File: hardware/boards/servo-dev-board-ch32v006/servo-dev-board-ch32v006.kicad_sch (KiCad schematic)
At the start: 87 parts, among them J1 BATT JST-PH, J2 BUS JST-ZH, J3 BUS JST-ZH, J4 SERVO JST-ZH, J5 ENC JST-ZH, J6 DBG JST-ZH, Q1 AO3401A, Q2 AO3401A, Q3 AO3401A, SW1 SW_Push, U1 TPAP2210K-3.3TRG1, U2 74LVC2G125RA3-7, U3 DRV8837DSGR-JSM, U4 CH32V006F8U6

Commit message: wip
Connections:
- net DATA: now also TP17.1; no longer TP4.1
- net DBG: now also TP16.1; no longer TP2.1
- net EN: now also TP14.1; no longer TP7.1
- net ENCA: now also TP8.1; no longer TP18.1
- net ENCB: now also TP9.1; no longer TP19.1
- net IN1: now also TP2.1; no longer TP5.1
- net IN2: now also TP3.1; no longer TP6.1
- net RX: now also TP18.1; no longer TP9.1
- net TX: now also TP19.1; no longer TP8.1
- net VNTC: now also TP7.1; no longer TP15.1
- net VPOS: now also TP6.1; no longer TP14.1
- net VSNA: now also TP4.1; no longer TP16.1
- net VSNB: now also TP5.1; no longer TP17.1
- net LED renamed STAT
- net STAT: now also TP15.1; no longer TP3.1
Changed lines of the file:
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@@
 	(wire
 		(pts
-			(xy 147.32 142.24) (xy 147.32 138.43)
+			(xy 147.32 142.24) (xy 147.32 135.89)
 		)
 		(stroke
@@
 		)
 	)
-	(label "LED"
-		(at 147.32 138.43 0)
-		(effects
-			(font
-				(size 1.27 1.27)
-			)
-			(justify left bottom)
+	(label "STAT"
+		(at 147.32 135.89 270)
+		(effects
+			(font
+				(size 1.27 1.27)
+			)
+			(justify right bottom)
 		)
 	)
@@
 		)
 	)
+	(label "RX"
+		(at 229.87 40.64 0)
+		(effects
+			(font
+				(size 1.27 1.27)
+			)
+			(justify left bottom)
+		)
+	)
+	(label "ENCB"
+		(at 226.06 43.18 180)
+		(effects
+			(font
+				(size 1.27 1.27)
+			)
+			(justify right bottom)
+		)
+	)
 	(label "ENCA"
 		(at 256.54 91.44 180)
@@
 		)
 	)
+	(label "VSNA"
+		(at 226.06 30.48 180)
+		(effects
+			(font
+				(size 1.27 1.27)
+			)
+			(justify right bottom)
+		)
+	)
 	(label "ISNS+"
 		(at 257.81 140.97 180)
@@
 	)
 	(label "ENCA"
-		(at 229.87 40.64 0)
-		(effects
-			(font
-				(size 1.27 1.27)
-			)
-			(justify left bottom)
+		(at 226.06 40.64 180)
+		(effects
+			(font
+				(size 1.27 1.27)
+			)
+			(justify right bottom)
 		)
 	)
@@
 		)
 	)
-	(label "ENCB"
-		(at 229.87 43.18 0)
-		(effects
-			(font
-				(size 1.27 1.27)
-			)
-			(justify left bottom)
-		)
-	)
-	(label "VPOS"
-		(at 229.87 30.48 0)
-		(effects
-			(font
-				(size 1.27 1.27)
-			)
-			(justify left bottom)
-		)
-	)
 	(label "VNTC"
 		(at 256.54 93.98 180)
@@
 		)
 	)
-	(label "DBG"
-		(at 226.06 25.4 180)
-		(effects
-			(font
-				(size 1.27 1.27)
-			)
-			(justify right bottom)
-		)
-	)
-	(label "DATA"
-		(at 226.06 30.48 180)
-		(effects
-			(font
-				(size 1.27 1.27)
-			)
-			(justify right bottom)
-		)
-	)
-	(label "LED"
+	(label "STAT"
 		(at 187.96 106.68 0)
 		(effects
@@
 		)
 	)
-	(label "LED"
-		(at 226.06 27.94 180)
+	(label "VPOS"
+		(at 226.06 35.56 180)
 		(effects
 			(font
@@
 		)
 	)
-	(label "IN1"
-		(at 226.06 33.02 180)
-		(effects
-			(font
-				(size 1.27 1.27)
-			)
-			(justify right bottom)
-		)
-	)
 	(label "GND"
 		(at 226.06 22.86 180)
@@
 		)
 	)
+	(label "DATA"
+		(at 229.87 38.1 0)
+		(effects
+			(font
+				(size 1.27 1.27)
+			)
+			(justify left bottom)
+		)
+	)
 	(label "OUTB"
 		(at 104.14 73.66 180)
@@
 		)
 	)
-	(label "VNTC"
+	(label "STAT"
 		(at 229.87 33.02 0)
 		(effects
@@
 		)
 	)
+	(label "IN1"
+		(at 226.06 25.4 180)
+		(effects
+			(font
+				(size 1.27 1.27)
+			)
+			(justify right bottom)
+		)
+	)
 	(label "ENCB"
 		(at 256.54 88.9 180)
@@
 		)
 	)
-	(label "TX"
-		(at 226.06 40.64 180)
-		(effects
-			(font
-				(size 1.27 1.27)
-			)
-			(justify right bottom)
-		)
-	)
 	(label "VSYS"
 		(at 63.5 38.1 0)
@@
 		)
 	)
-	(label "RX"
-		(at 226.06 43.18 180)
-		(effects
-			(font
-				(size 1.27 1.27)
-			)
-			(justify right bottom)
-		)
-	)
 	(label "BUF"
 		(at 167.64 41.91 180)
@@
 		)
 	)
+	(label "EN"
+		(at 229.87 30.48 0)
+		(effects
+			(font
+				(size 1.27 1.27)
+			)
+			(justify left bottom)
+		)
+	)
 	(label "VSNB"
 		(at 256.54 96.52 180)
@@
 		)
 	)
-	(label "IN2"
-		(at 226.06 35.56 180)
+	(label "VNTC"
+		(at 226.06 38.1 180)
 		(effects
 			(font
@@
 		)
 	)
+	(label "IN2"
+		(at 226.06 27.94 180)
+		(effects
+			(font
+				(size 1.27 1.27)
+			)
+			(justify right bottom)
+		)
+	)
 	(label "OUTB"
 		(at 247.65 31.75 0)
@@
 		)
 	)
-	(label "EN"
-		(at 226.06 38.1 180)
-		(effects
-			(font
-				(size 1.27 1.27)
-			)
-			(justify right bottom)
-		)
-	)
 	(label "SWDIO"
 		(at 256.54 101.6 180)
@@
 		)
 	)
+	(label "DBG"
+		(at 229.87 35.56 0)
+		(effects
+			(font
+				(size 1.27 1.27)
+			)
+			(justify left bottom)
+		)
+	)
 	(label "RX"
 		(at 137.16 41.91 0)
@@
 		)
 	)
-	(label "VSNA"
-		(at 229.87 35.56 0)
-		(effects
-			(font
-				(size 1.27 1.27)
-			)
-			(justify left bottom)
-		)
-	)
 	(label "VPOS"
 		(at 256.54 99.06 180)
@@
 		)
 	)
-	(label "VSNB"
-		(at 229.87 38.1 0)
-		(effects
-			(font
-				(size 1.27 1.27)
-			)
-			(justify left bottom)
-		)
-	)
 	(label "OUTA"
 		(at 97.79 149.86 180)
@@
 		)
 	)
+	(label "VSNB"
+		(at 226.06 33.02 180)
+		(effects
+			(font
+				(size 1.27 1.27)
+			)
+			(justify right bottom)
+		)
+	)
 	(label "OUTB"
 		(at 97.79 152.4 180)
@@
 	(label "3V3_DRV"
 		(at 212.09 57.15 0)
+		(effects
+			(font
+				(size 1.27 1.27)
+			)
+			(justify left bottom)
+		)
+	)
+	(label "TX"
+		(at 229.87 43.18 0)
 		(effects
 			(font
@@
 		(on_board yes)
 		(dnp no)
-		(fields_autoplaced yes)
 		(property "Reference" "#PWR0123"
 			(at 133.35 144.78 0)
@@
 		)
 		(property "Value" "+3.3V"
-			(at 133.35 135.89 0)
-			(effects
-				(font
-					(size 1.27 1.27)
-				)
+			(at 133.35 137.16 0)
+			(effects
+				(font
+					(size 1.27 1.27)
+				)
+				(justify bottom)
 			)
 		)
@@
 		)
 		(property "Value" "VSYS"
-			(at 117.856 136.652 0)
-			(effects
-				(font
-					(size 1.27 1.27)
-				)
-			)
-		)
+			(at 118.11 137.16 0)
+			(effects
+				(font
+					(size 1.27 1.27)
+				)
+				(justify bottom)
+			)
+		)

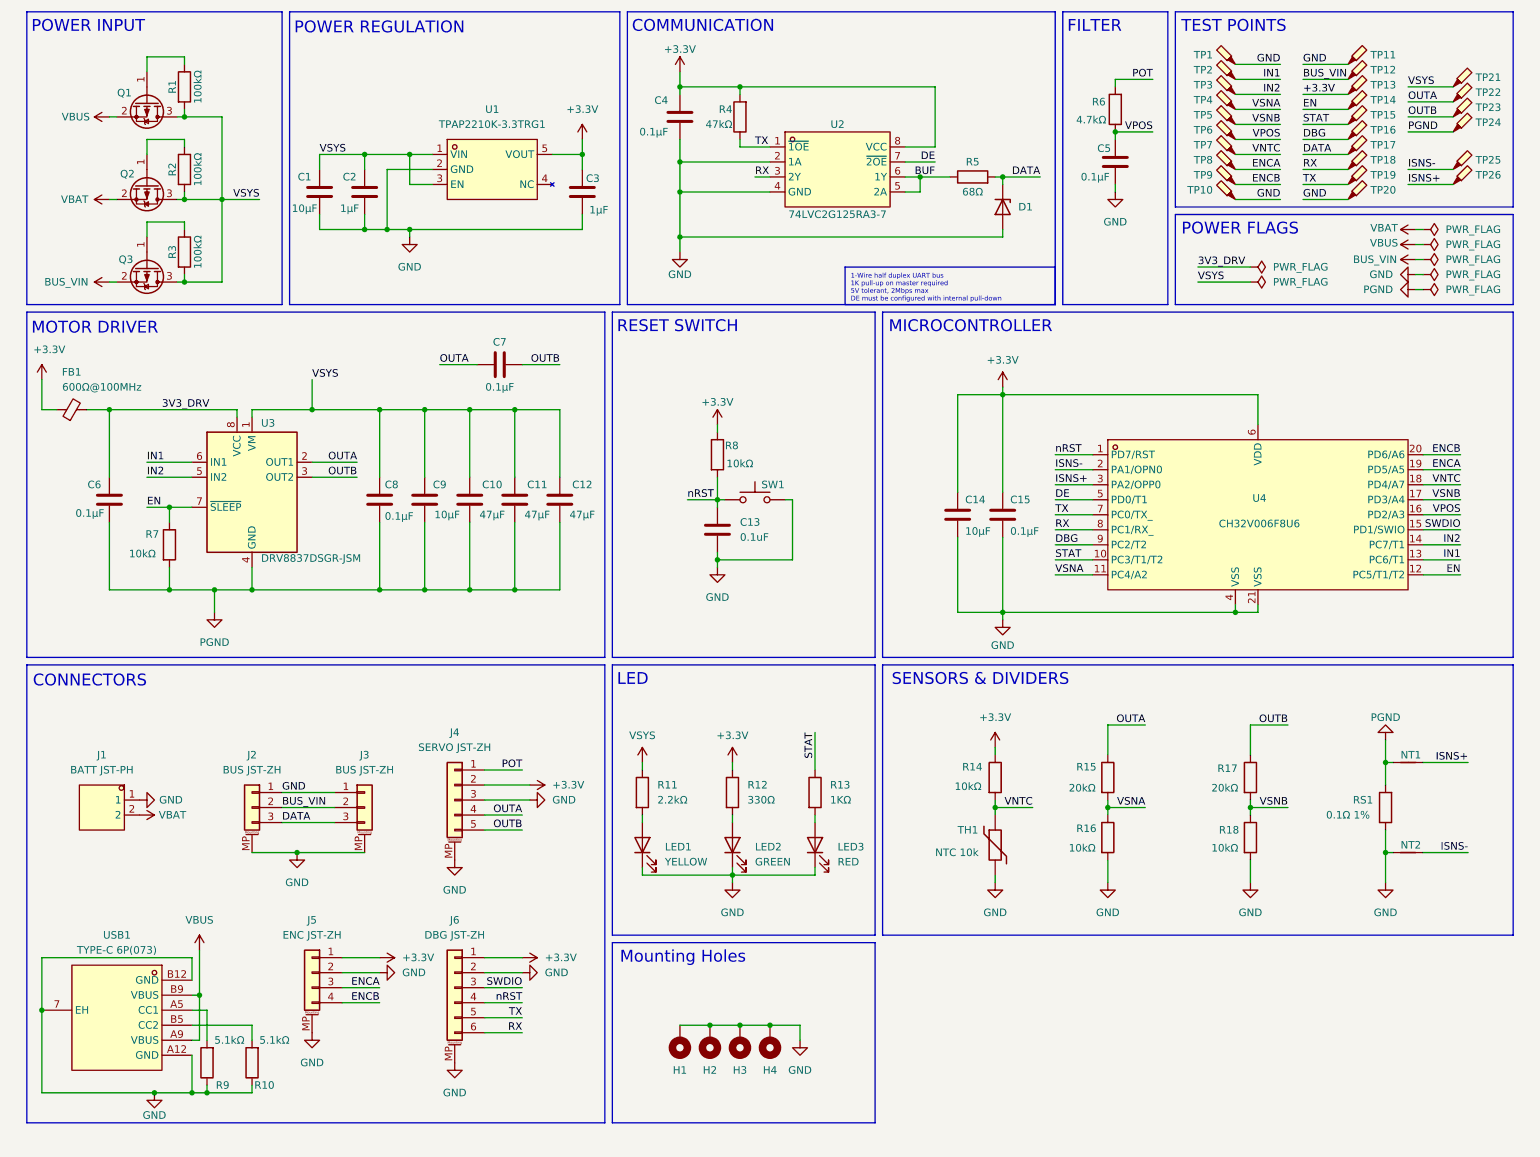
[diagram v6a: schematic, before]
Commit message: fixed battery connector pin outs. Added JLCPCB parts and produced production and gerber files
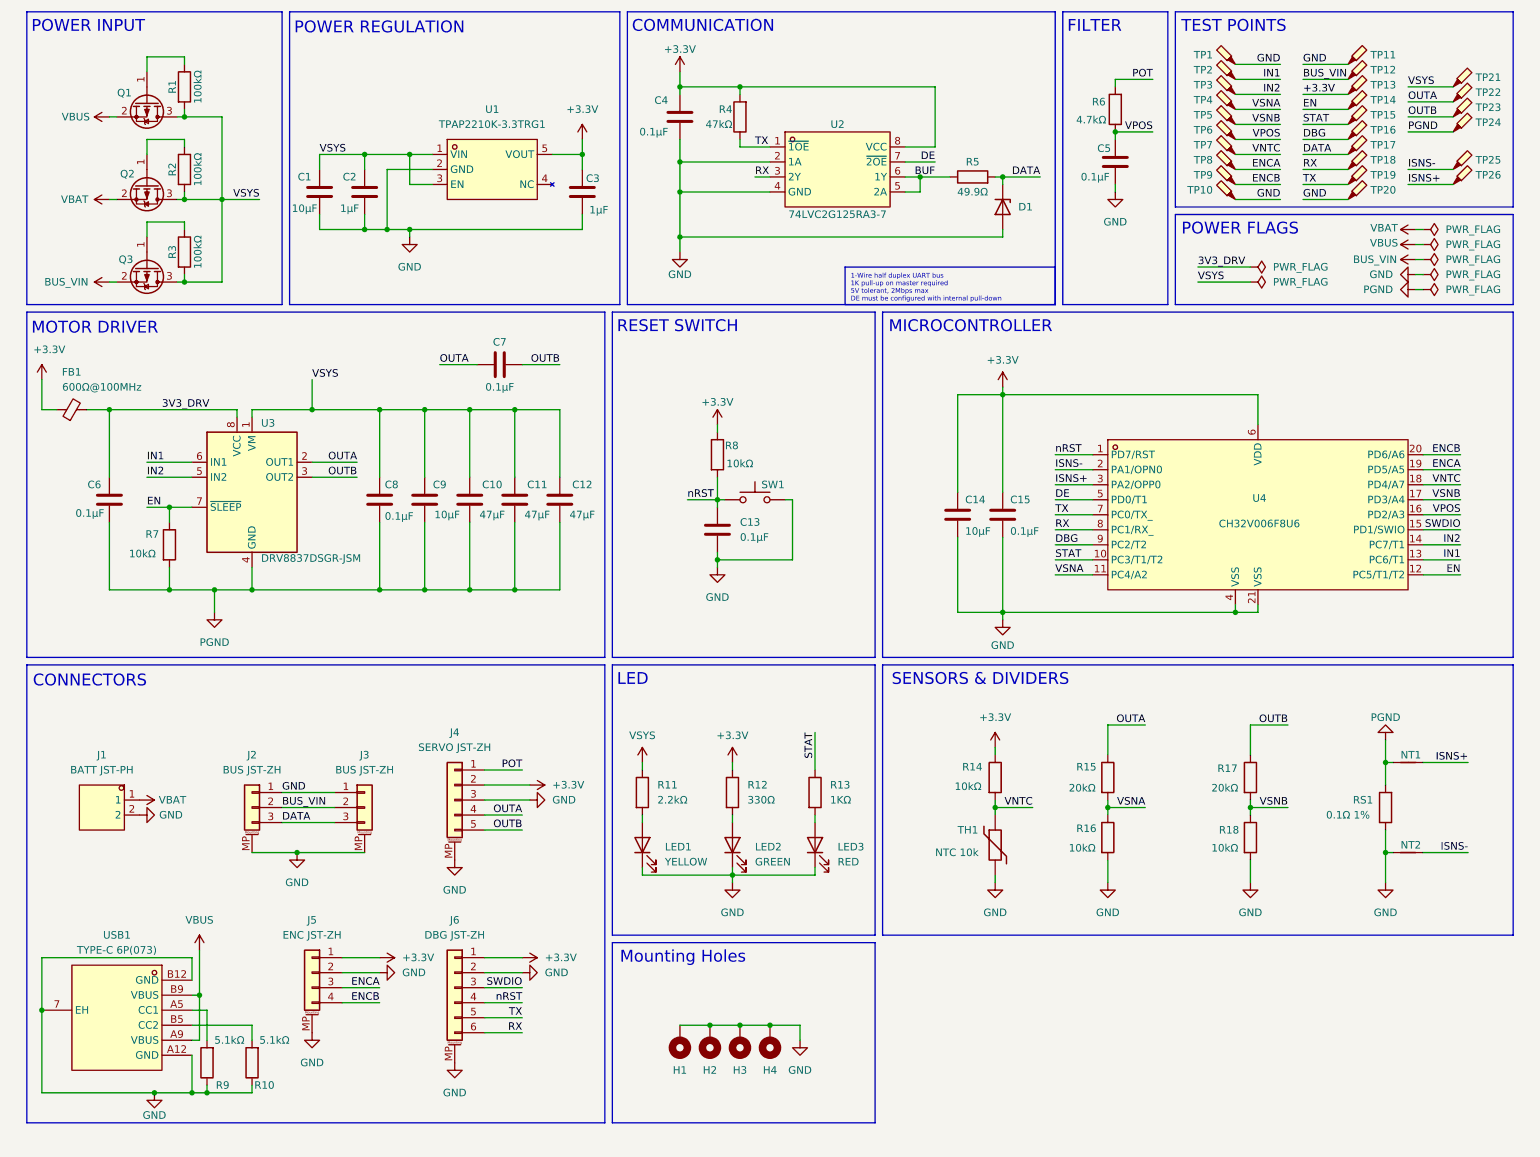
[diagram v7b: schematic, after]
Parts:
- C13: value 0.1uF -> 0.1µF
- C14: LCSC C1525 -> C96446
- C15, C4, C5, C6, C7, C8: LCSC C1525 -> C307331
- J1: LCSC (none) -> C173752
- J2, J3: LCSC (none) -> C489717
- J4: LCSC (none) -> C485355
- J5: LCSC (none) -> C485354
- J6: LCSC (none) -> C265070
- R1, R2, R3: LCSC C25744 -> C25741
- R10, R9: LCSC C25744 -> C25905
- R11: LCSC C25792 -> C25879
- R12: LCSC C25792 -> C25104
- R13: LCSC C25792 -> C11702
- R15, R17: LCSC C25764 -> C25765
- R5: value 68Ω -> 49.9Ω; LCSC C25792 -> C25120
- SW1: LCSC C221895 -> C2681476
- TP10, TP11, TP12, TP13, TP14, TP15, TP16, TP17, TP18, TP19, TP2, TP20, TP21, TP22, TP23, TP24, TP25, TP26, TP3, TP4, TP5, TP6, TP7, TP8, TP9: LCSC (none) -> C5199798
- U2: LCSC (none) -> C842614
- USB1: LCSC (none) -> C668623
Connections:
- net GND: now also J1.2; no longer J1.1
- net VBAT: now also J1.1; no longer J1.2

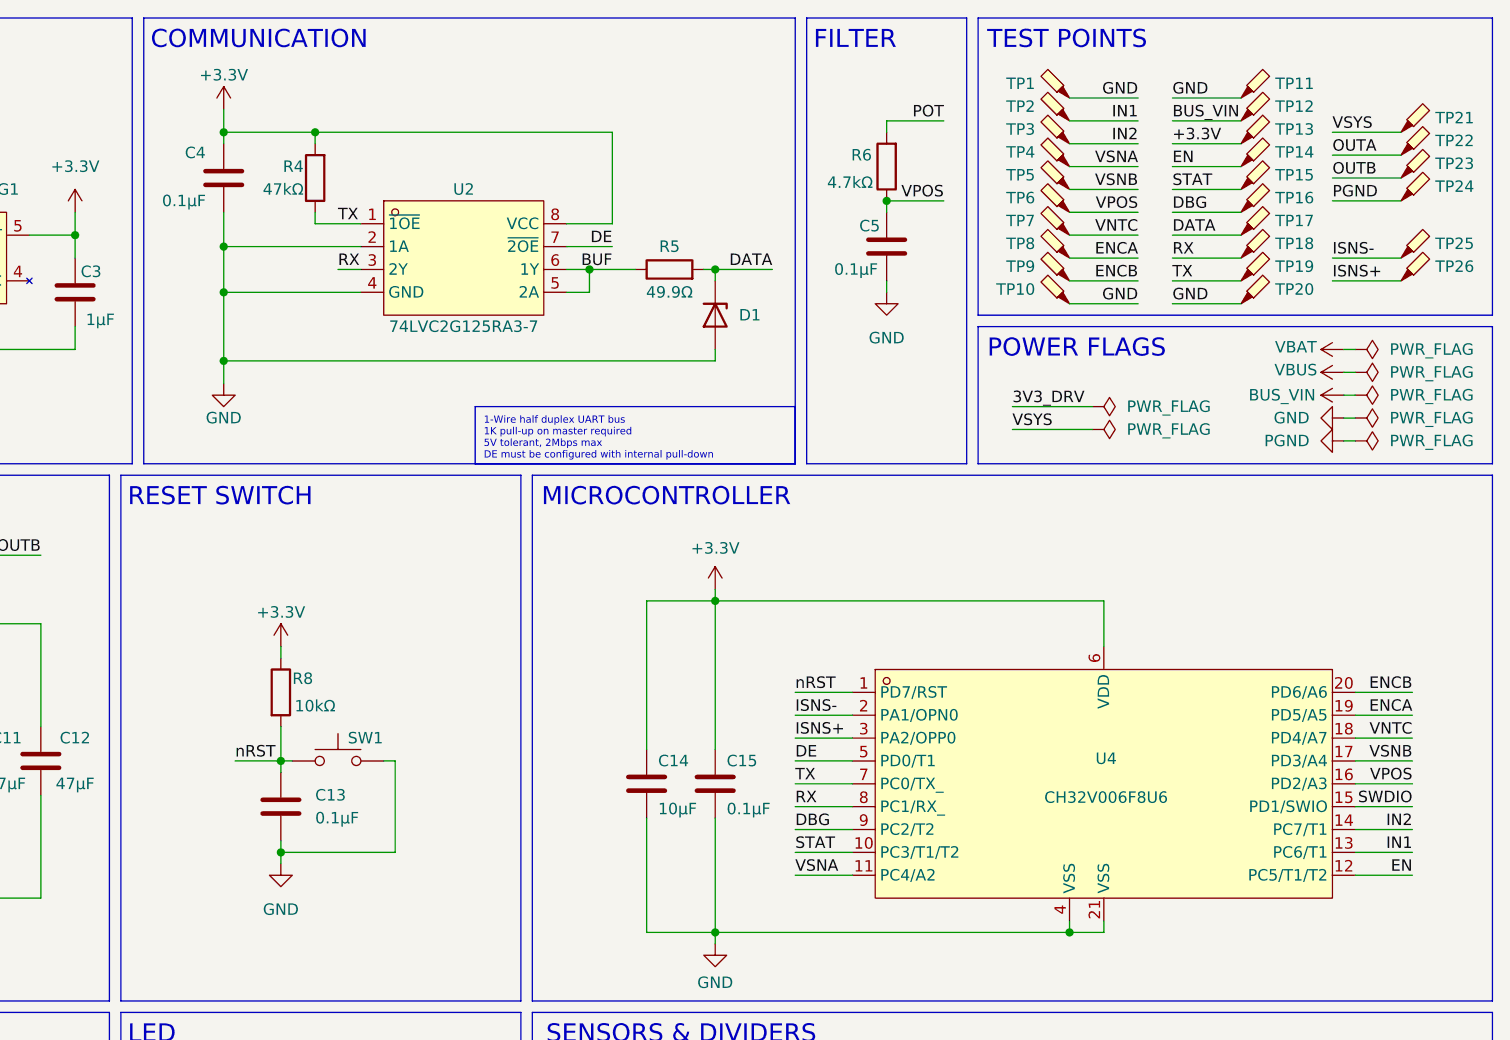
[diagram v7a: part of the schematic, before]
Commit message: routing ADC nets with higher priority so that measurements stay clean
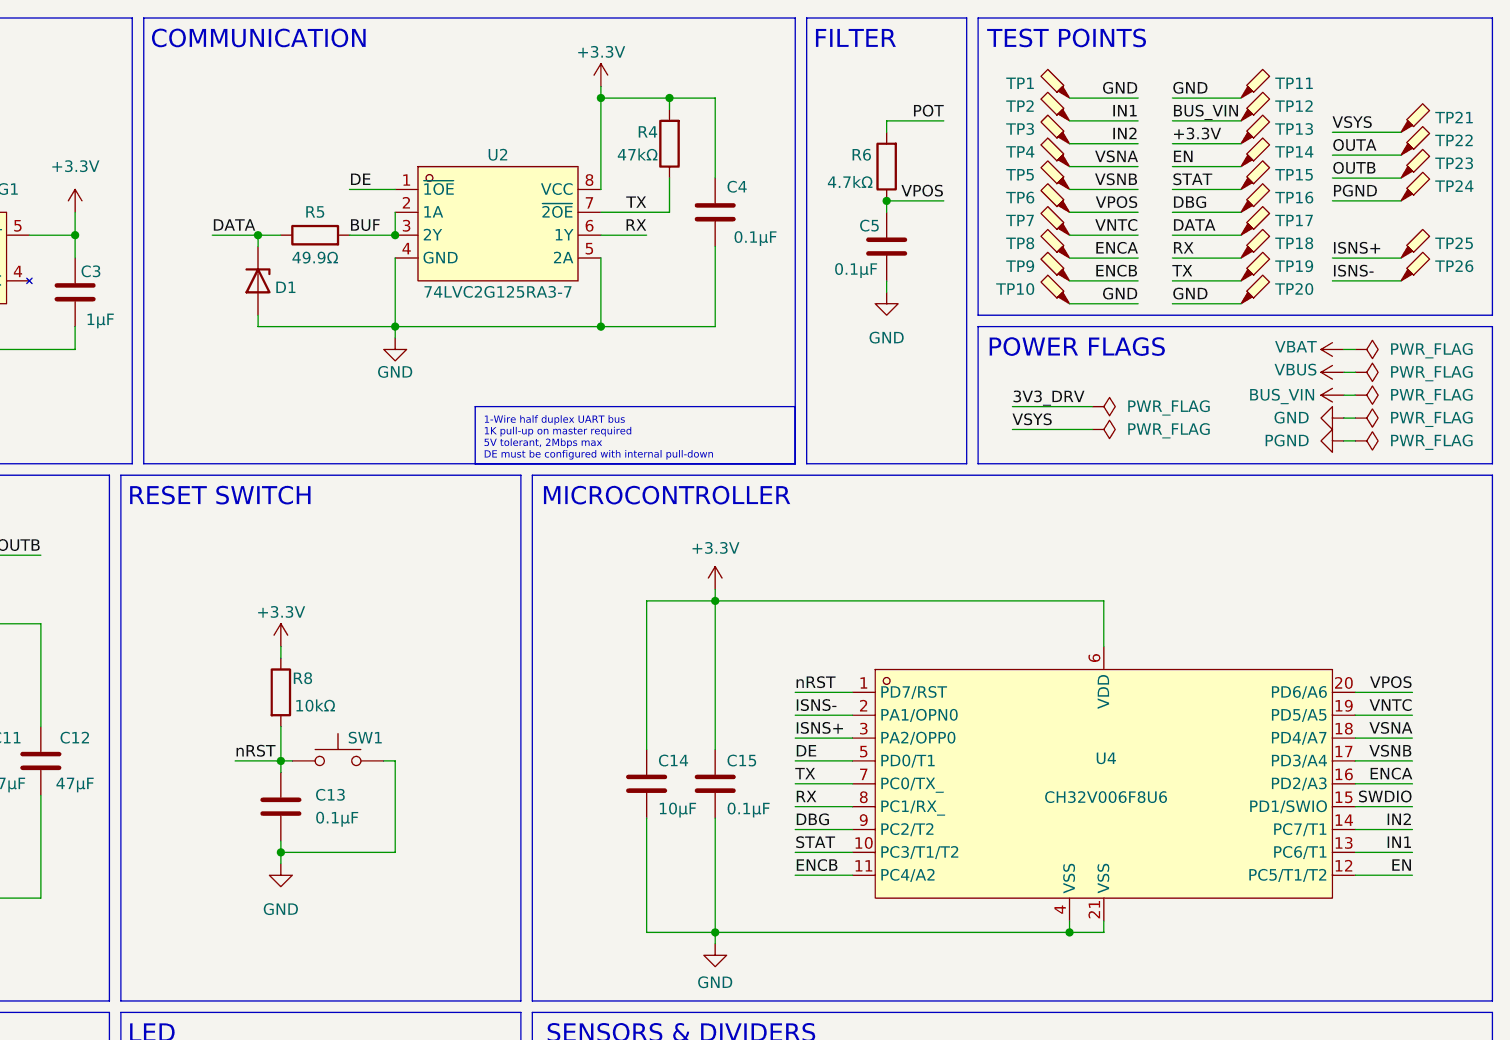
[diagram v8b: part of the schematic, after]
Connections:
- net BUF: now also R5.2, U2.2 (1A), U2.3 (2Y); no longer R5.1, U2.5 (2A), U2.6 (1Y)
- net DATA: now also R5.1; no longer R5.2
- net DE: now also U2.1 (~{1OE}); no longer U2.7 (~{2OE})
- net ENCA: now also U4.16 (PD2/A3); no longer U4.19 (PD5/A5)
- net ENCB: now also U4.11 (PC4/A2); no longer U4.20 (PD6/A6)
- net GND: now also U2.5 (2A); no longer U2.2 (1A)
- net ISNS+: now also TP25.1; no longer TP26.1
- net ISNS-: now also TP26.1; no longer TP25.1
- net RX: now also U2.6 (1Y); no longer U2.3 (2Y)
- net TX: now also U2.7 (~{2OE}); no longer U2.1 (~{1OE})
- net VNTC: now also U4.19 (PD5/A5); no longer U4.18 (PD4/A7)
- net VPOS: now also U4.20 (PD6/A6); no longer U4.16 (PD2/A3)
- net VSNA: now also U4.18 (PD4/A7); no longer U4.11 (PC4/A2)
